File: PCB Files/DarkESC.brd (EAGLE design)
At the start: 83.3 x 79.7 mm, 98 parts, among them IC1 7805DT, IC2 ACS712ELCTR-20A-T, Q1 BC817-40W, Q2 BC817-40W, Q3 BC817-40W, Q4 IRF520, Q5 IRF520, Q6 IRF520, Q7 IRF520, Q8 IRF520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

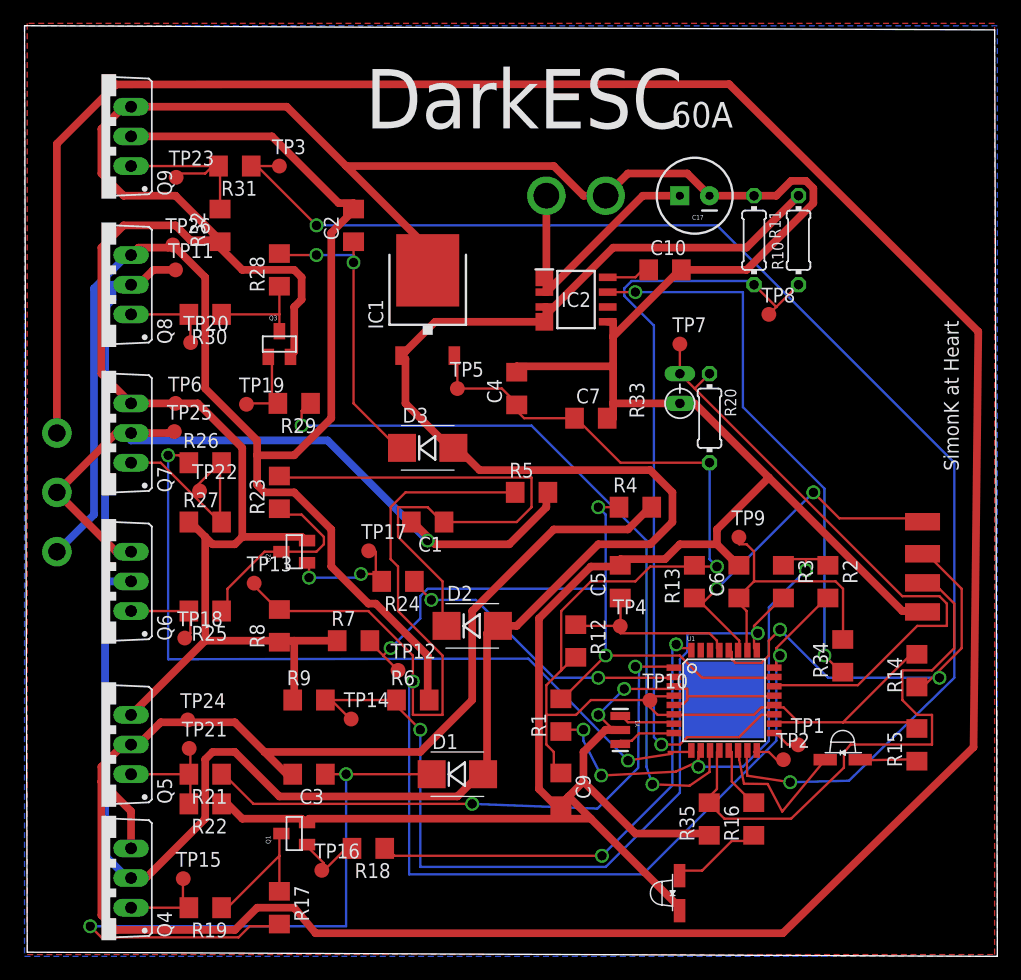
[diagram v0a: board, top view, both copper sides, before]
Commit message: Fixed Dimension
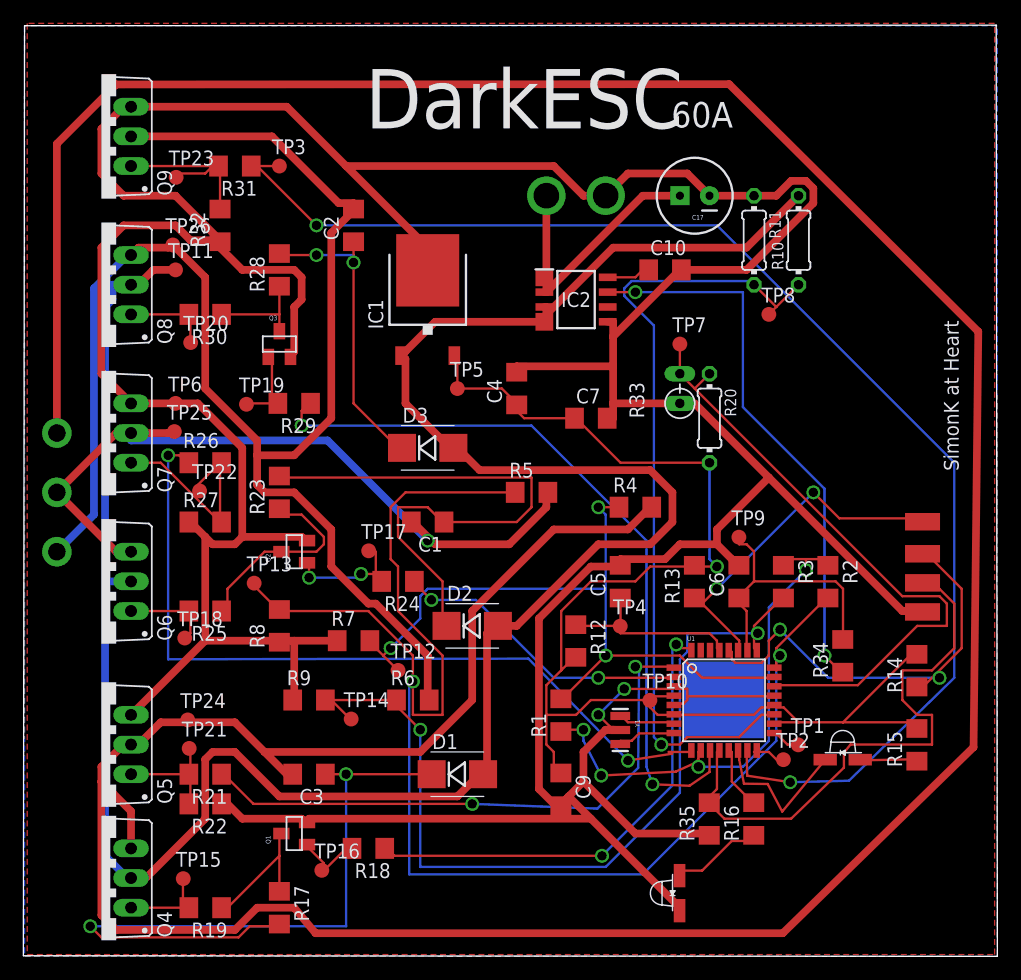
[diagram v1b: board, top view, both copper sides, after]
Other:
- board size 83.3 x 79.7 mm -> 83.4 x 79.7 mm
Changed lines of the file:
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@@
 <drawing>
 <settings>
-<setting alwaysvectorfont="yes"/>
+<setting alwaysvectorfont="no"/>
 <setting verticaltext="up"/>
 </settings>
@@
 <board>
 <plain>
-<wire x1="0" y1="0" x2="83.0634" y2="-0.3556" width="0" layer="20"/>
-<wire x1="83.0634" y1="-0.3556" x2="82.8348" y2="78.9688" width="0" layer="20"/>
-<wire x1="82.8348" y1="78.9688" x2="-0.2286" y2="79.3244" width="0" layer="20"/>
-<wire x1="-0.2286" y1="79.3244" x2="0" y2="0" width="0" layer="20"/>
+<wire x1="-0.3302" y1="-0.3048" x2="83.0634" y2="-0.3556" width="0" layer="20"/>
+<wire x1="83.0634" y1="-0.3556" x2="82.9618" y2="79.3752" width="0" layer="20"/>
+<wire x1="82.9618" y1="79.3752" x2="-0.2286" y2="79.3244" width="0" layer="20"/>
+<wire x1="-0.2286" y1="79.3244" x2="-0.3302" y2="-0.3048" width="0" layer="20"/>
 <rectangle x1="56.2102" y1="18.3134" x2="63.0682" y2="24.892" layer="16"/>
 <text x="42.545" y="73.0758" size="5.08" layer="21" font="vector" align="center">DarkESC</text>
